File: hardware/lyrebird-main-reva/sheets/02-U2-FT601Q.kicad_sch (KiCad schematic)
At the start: 19 parts, among them Q1 BSS138, U2 FT601Q, Y1 ABM8G-30.000MHZ-18-D2Y-T

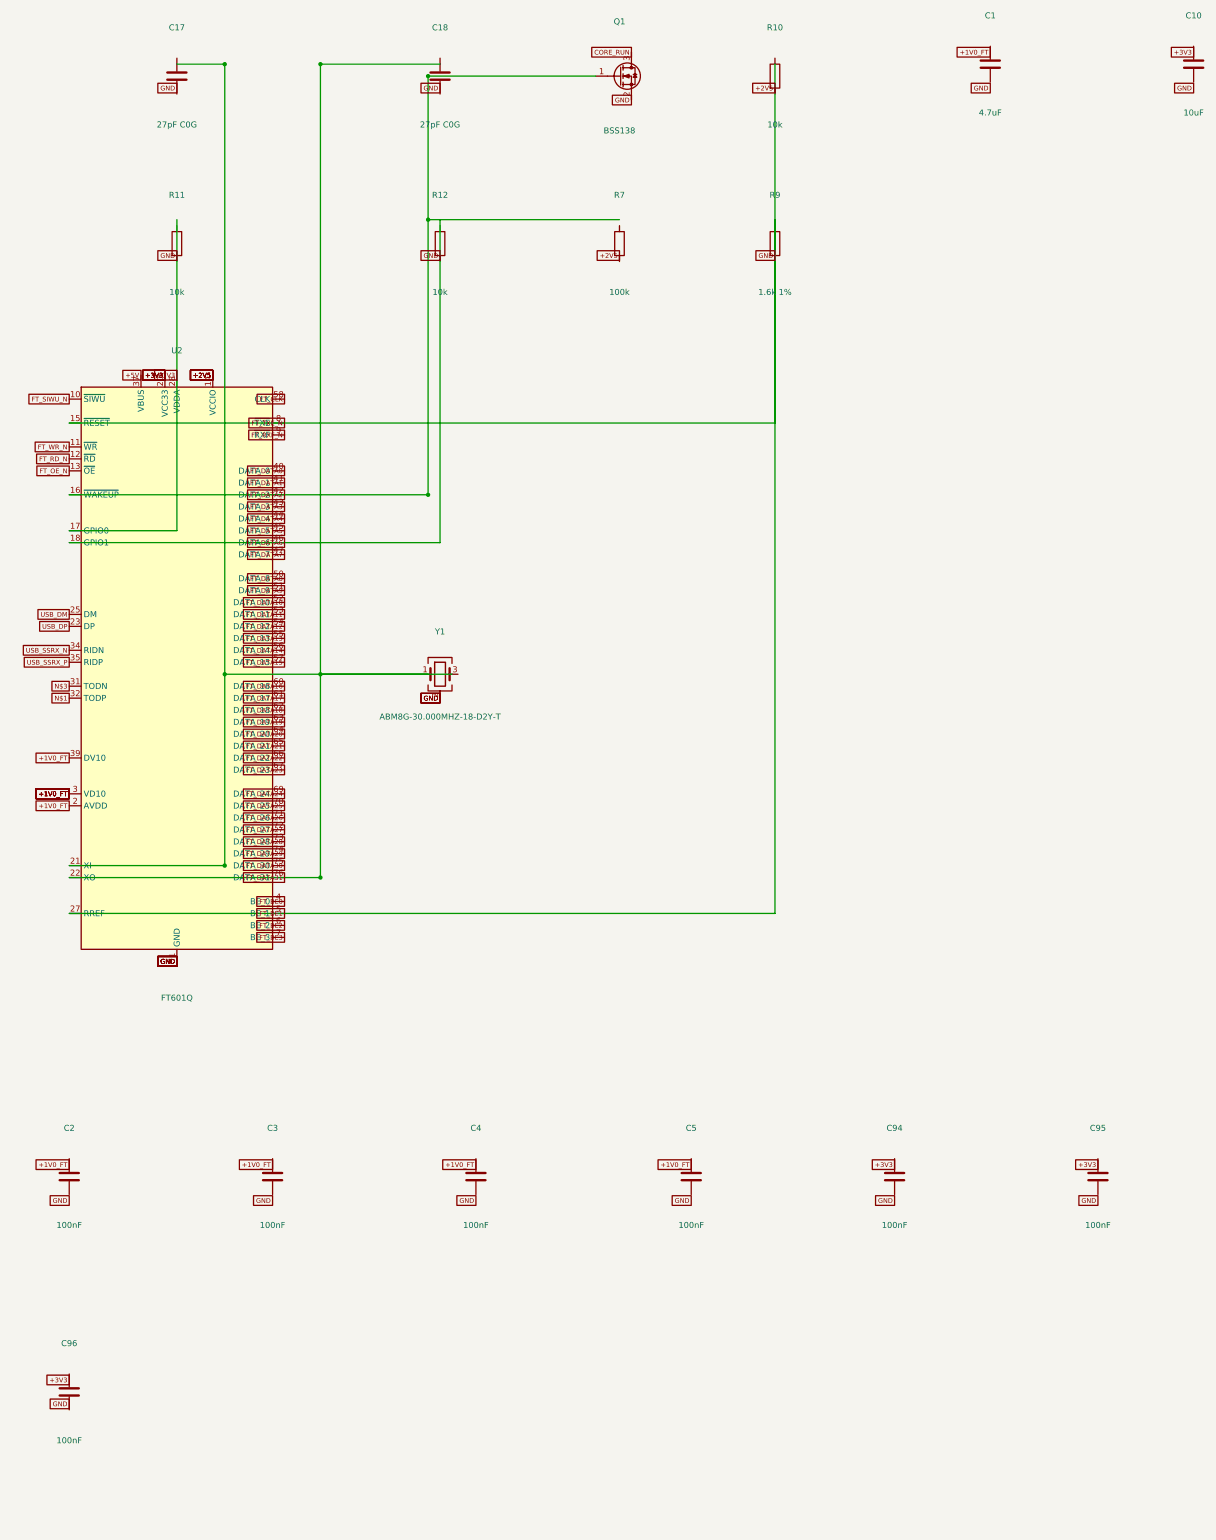
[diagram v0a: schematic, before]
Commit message: Regenerate the schematics, which were eleven days behind the netlists
The sheets and both PDFs dated 13 September against netlists from
today. They showed a board with USB bus power, a charge pump on the
analog module, no JTAG series protection, no oscillator pull-downs and
none of the footprint corrections -- a board that has not existed for
some time. Anyone opening them to review the design would have been
reviewing the wrong one, which is worse than having no schematic.

Regenerated from the current netlists: the main board goes from 8
sheets to 11, picking up the wall-wart input and the inverter, and the
module from 6 to 9 while losing the charge pump entirely. Both PDFs
rebuilt through kicad-cli, one page per sheet.

Nothing regenerated them because nothing was watching. The netlist
generators are run constantly and the views derived from them are not,
so they drift silently and there is no check that notices.

Co-Authored-By: Claude Opus 5 <noreply@anthropic.com>
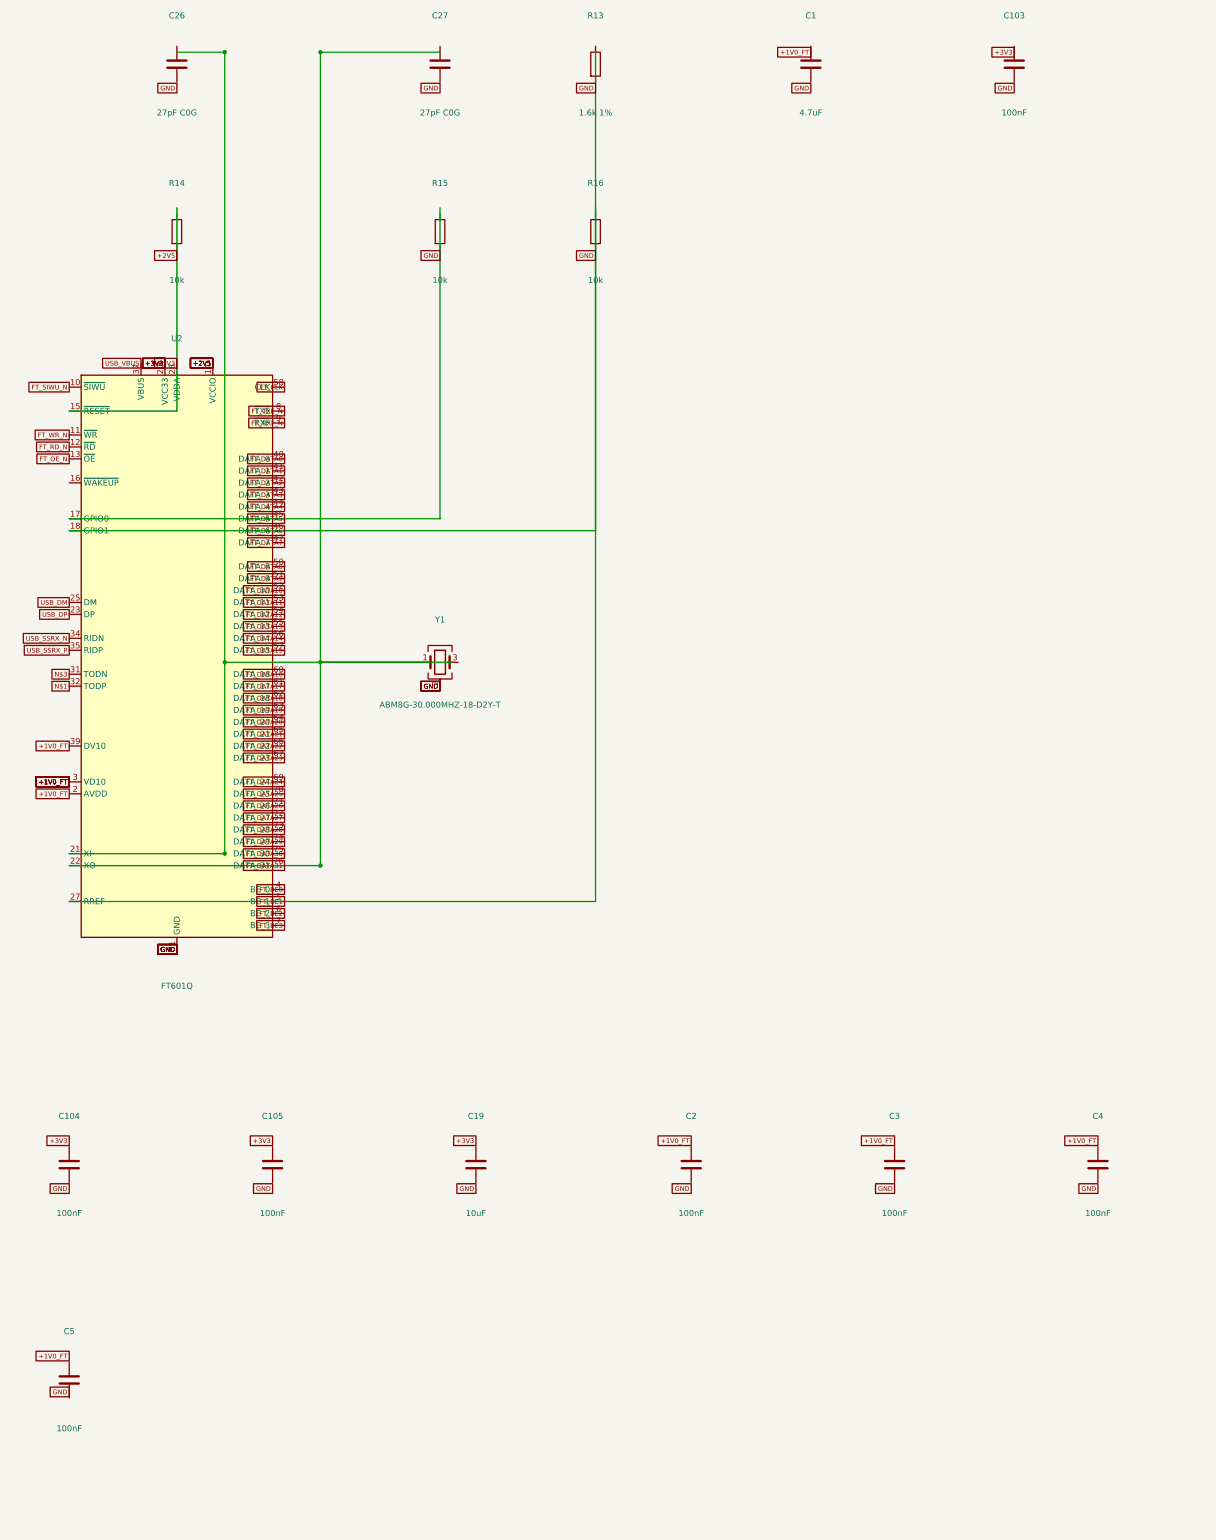
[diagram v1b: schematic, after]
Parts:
- removed C95, C96: 100nF, symbol Device:C
- C1: renamed from U2; value FT601Q -> 4.7uF; symbol Interface_USB:FT601Q -> Device:C
- C103: renamed from Y1; value ABM8G-30.000MHZ-18-D2Y-T -> 100nF; symbol Device:Crystal_GND24 -> Device:C
- C104: renamed from C1; value 4.7uF -> 100nF
- C105: renamed from C10; value 10uF -> 100nF
- C19: renamed from C2; value 100nF -> 10uF
- R13: renamed from Q1; value BSS138 -> 1.6k 1%; symbol Transistor_FET:BSS138 -> Device:R
- U2: renamed from R7; value 100k -> FT601Q; symbol Device:R -> Interface_USB:FT601Q
- Y1: renamed from R9; value 1.6k 1% -> ABM8G-30.000MHZ-18-D2Y-T; symbol Device:R -> Device:Crystal_GND24
- renumbered C3 to C2, C17 to C26, C18 to C27, C4 to C3, C5 to C4, C94 to C5, R10 to R14, R11 to R15, R12 to R16
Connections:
- net +1V0_FT: now also U2.2 (AVDD), U2.3 (VD10), U2.30 (VD10), U2.33 (VD10), U2.39 (DV10), U2.48 (VD10); no longer C1.2 (AVDD), C1.3 (VD10), C1.30 (VD10), C1.33 (VD10), C1.39 (DV10), C1.48 (VD10)
- net +2V5: now also U2.14 (VCCIO), U2.15 (~{RESET}), U2.20 (VCC33), U2.24 (VCC33), U2.28 (VDDA), U2.38 (VCC33), U2.49 (VCCIO), U2.59 (VCCIO), U2.68 (VCCIO); no longer C1.1 (GND), C1.14 (VCCIO), C1.15 (~{RESET}), C1.17 (GPIO0), C1.18 (GPIO1), C1.20 (VCC33), C1.24 (VCC33), C1.26 (GND), C1.27 (RREF), C1.28 (VDDA), C1.29 (GND), C1.36 (GND), C1.38 (VCC33), C1.46 (DATA_6), C1.49 (VCCIO), C1.5 (BE_1), C1.59 (VCCIO), C1.68 (VCCIO), C1.77 (GND), C1.8 (~{TXE}), C103.2 (G), C103.4 (G), R13.2 (S)
- net FT_BE0: now also U2.4 (BE_0); no longer C1.4 (BE_0)
- net FT_BE2: now also U2.6 (BE_2); no longer C1.6 (BE_2)
- net FT_BE3: now also U2.7 (BE_3); no longer C1.7 (BE_3)
- net FT_CLK: now also U2.58 (CLK); no longer C1.58 (CLK)
- net FT_DATA0: now also U2.40 (DATA_0); no longer C1.40 (DATA_0)
- net FT_DATA1: now also U2.41 (DATA_1); no longer C1.41 (DATA_1)
- net FT_DATA10: now also U2.52 (DATA_10); no longer C1.52 (DATA_10)
- net FT_DATA11: now also U2.53 (DATA_11); no longer C1.53 (DATA_11)
- net FT_DATA12: now also U2.54 (DATA_12); no longer C1.54 (DATA_12)
- net FT_DATA13: now also U2.55 (DATA_13); no longer C1.55 (DATA_13)
- net FT_DATA14: now also U2.56 (DATA_14); no longer C1.56 (DATA_14)
- net FT_DATA15: now also U2.57 (DATA_15); no longer C1.57 (DATA_15)
- net FT_DATA16: now also U2.60 (DATA_16); no longer C1.60 (DATA_16)
- net FT_DATA17: now also U2.61 (DATA_17); no longer C1.61 (DATA_17)
- net FT_DATA18: now also U2.62 (DATA_18); no longer C1.62 (DATA_18)
- net FT_DATA19: now also U2.63 (DATA_19); no longer C1.63 (DATA_19)
- net FT_DATA2: now also U2.42 (DATA_2); no longer C1.16 (~{WAKEUP}), C1.42 (DATA_2), R13.1 (G)
- net FT_DATA20: now also U2.64 (DATA_20); no longer C1.64 (DATA_20)
- net FT_DATA21: now also U2.65 (DATA_21); no longer C1.65 (DATA_21)
- net FT_DATA22: now also U2.66 (DATA_22); no longer C1.66 (DATA_22)
- net FT_DATA23: now also U2.67 (DATA_23); no longer C1.67 (DATA_23)
- net FT_DATA24: now also U2.69 (DATA_24); no longer C1.69 (DATA_24)
- net FT_DATA25: now also U2.70 (DATA_25); no longer C1.70 (DATA_25)
- net FT_DATA26: now also U2.71 (DATA_26); no longer C1.71 (DATA_26)
- net FT_DATA27: now also U2.72 (DATA_27); no longer C1.72 (DATA_27)
- net FT_DATA28: now also U2.73 (DATA_28); no longer C1.73 (DATA_28)
- net FT_DATA29: now also U2.74 (DATA_29); no longer C1.74 (DATA_29)
- net FT_DATA3: now also U2.43 (DATA_3); no longer C1.43 (DATA_3)
- net FT_DATA30: now also U2.75 (DATA_30); no longer C1.75 (DATA_30)
- net FT_DATA31: now also U2.21 (XI), U2.22 (XO), U2.76 (DATA_31); no longer C1.21 (XI), C1.22 (XO), C1.76 (DATA_31)
- net FT_DATA4: now also U2.44 (DATA_4); no longer C1.44 (DATA_4)
- net FT_DATA7: now also U2.47 (DATA_7); no longer C1.47 (DATA_7)
- net FT_DATA8: now also U2.50 (DATA_8); no longer C1.50 (DATA_8)
- net FT_DATA9: now also U2.51 (DATA_9); no longer C1.51 (DATA_9)
- net FT_OE_N: now also U2.13 (~{OE}); no longer C1.13 (~{OE})
- net FT_RD_N: now also U2.12 (~{RD}); no longer C1.12 (~{RD})
- net FT_RXF_N: now also U2.9 (~{RXF}); no longer C1.9 (~{RXF})
- net FT_SIWU_N: now also U2.10 (~{SIWU}); no longer C1.10 (~{SIWU})
- net FT_WR_N: now also U2.11 (~{WR}); no longer C1.11 (~{WR})
- net N$1: now also U2.32 (TODP); no longer C1.32 (TODP)
- net N$3: now also U2.31 (TODN); no longer C1.31 (TODN)
- net USB_DM: now also U2.25 (DM); no longer C1.25 (DM)
- net USB_DP: now also U2.23 (DP); no longer C1.23 (DP)
- net USB_SSRX_N: now also U2.34 (RIDN); no longer C1.34 (RIDN)
- net USB_SSRX_P: now also U2.35 (RIDP); no longer C1.35 (RIDP)
- net FT_BE1: now reaches U2.1 (GND)
- net FT_BE1: now also U2.17 (GPIO0), U2.18 (GPIO1), U2.26 (GND), U2.27 (RREF), U2.29 (GND), U2.36 (GND), U2.45 (DATA_5), U2.46 (DATA_6), U2.5 (BE_1), U2.77 (GND), Y1.2 (G), Y1.4 (G)
- removed net +5V: C1.37 (VBUS)
- removed net CORE_RUN: R13.3 (D)
- removed net FT_DATA5: C1.45 (DATA_5)
- new net FT_TXE_N: U2.8 (~{TXE})
- new net USB_VBUS: U2.37 (VBUS)
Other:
- moved on the sheet: C104, C105, C19, C2, C26, C27, C3, C4, C5, R14, R15, R16
